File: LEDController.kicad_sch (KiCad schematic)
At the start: 16 parts, among them J1 3557-2, J10 3557-2, J11 TB001-500-04BE, J12 TB001-500-04BE, J13 TB001-500-04BE, J14 TB001-500-04BE, J15 TB001-500-04BE, J2 3557-2, J3 3557-2, J4 3557-2, J5 3557-2, J6 3557-2, J7 3557-2, J8 3557-2, J9 3557-2

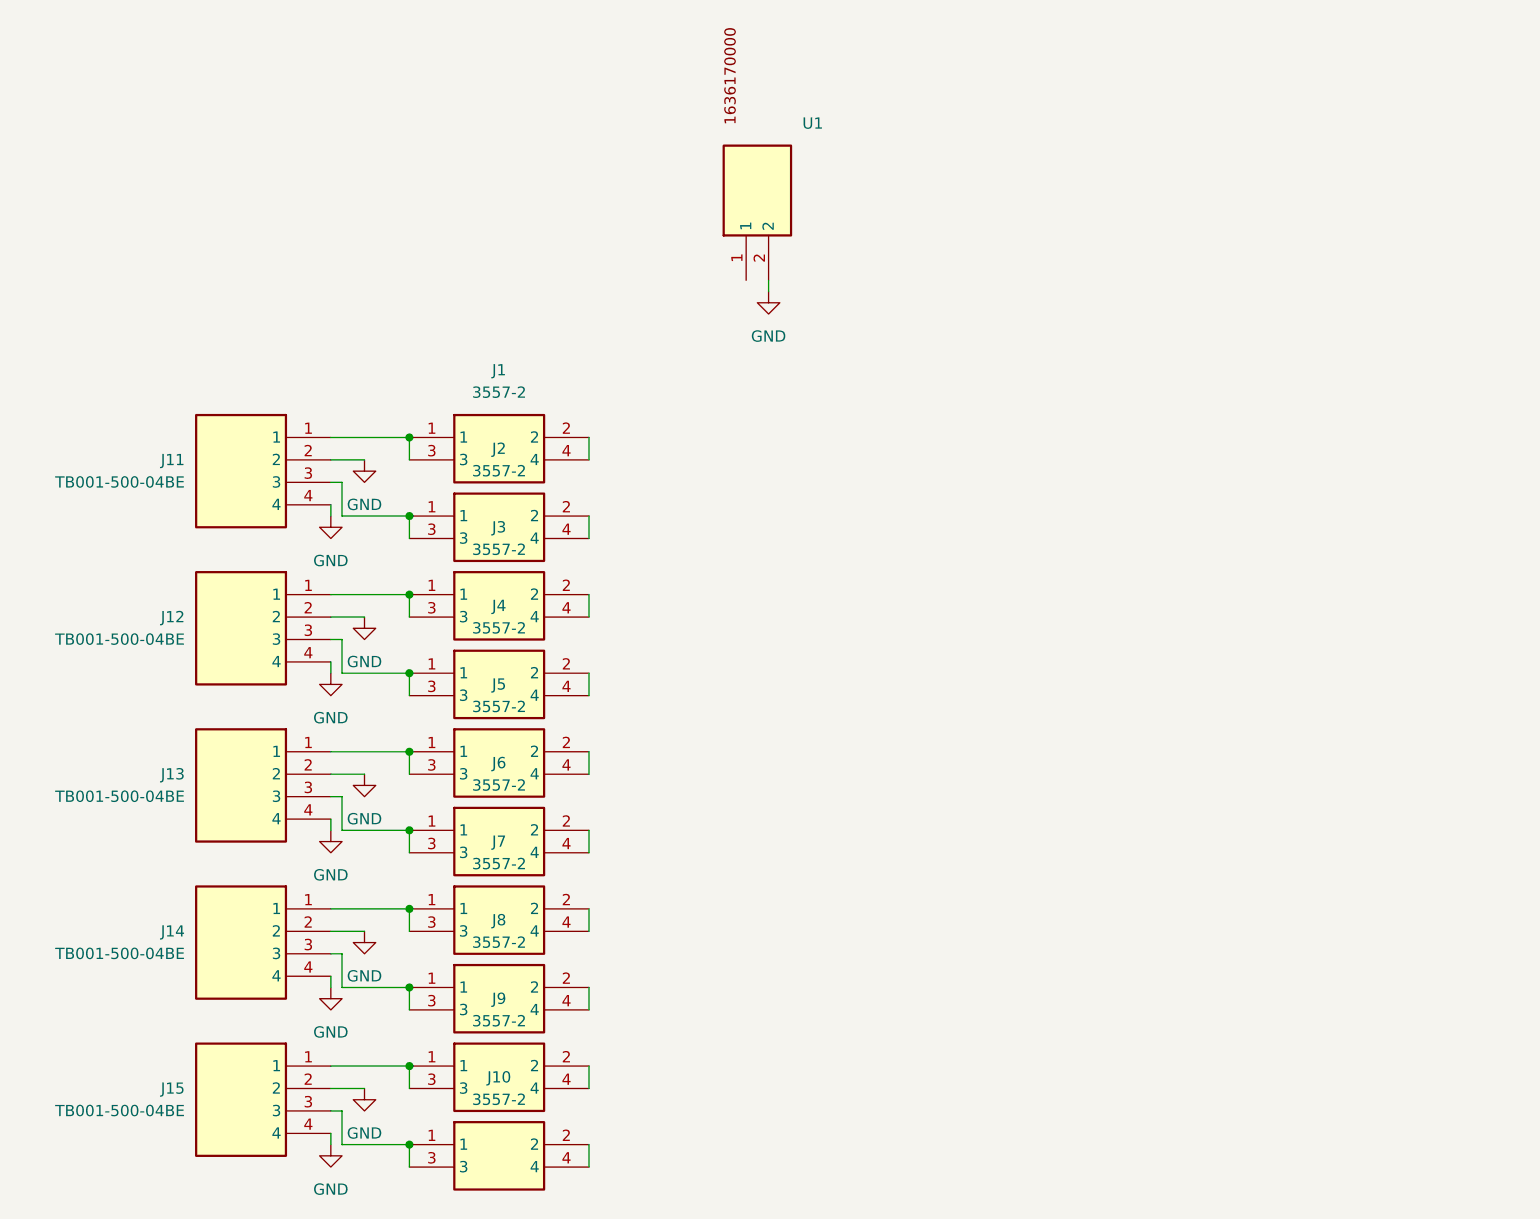
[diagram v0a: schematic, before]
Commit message: Added diode and transistor
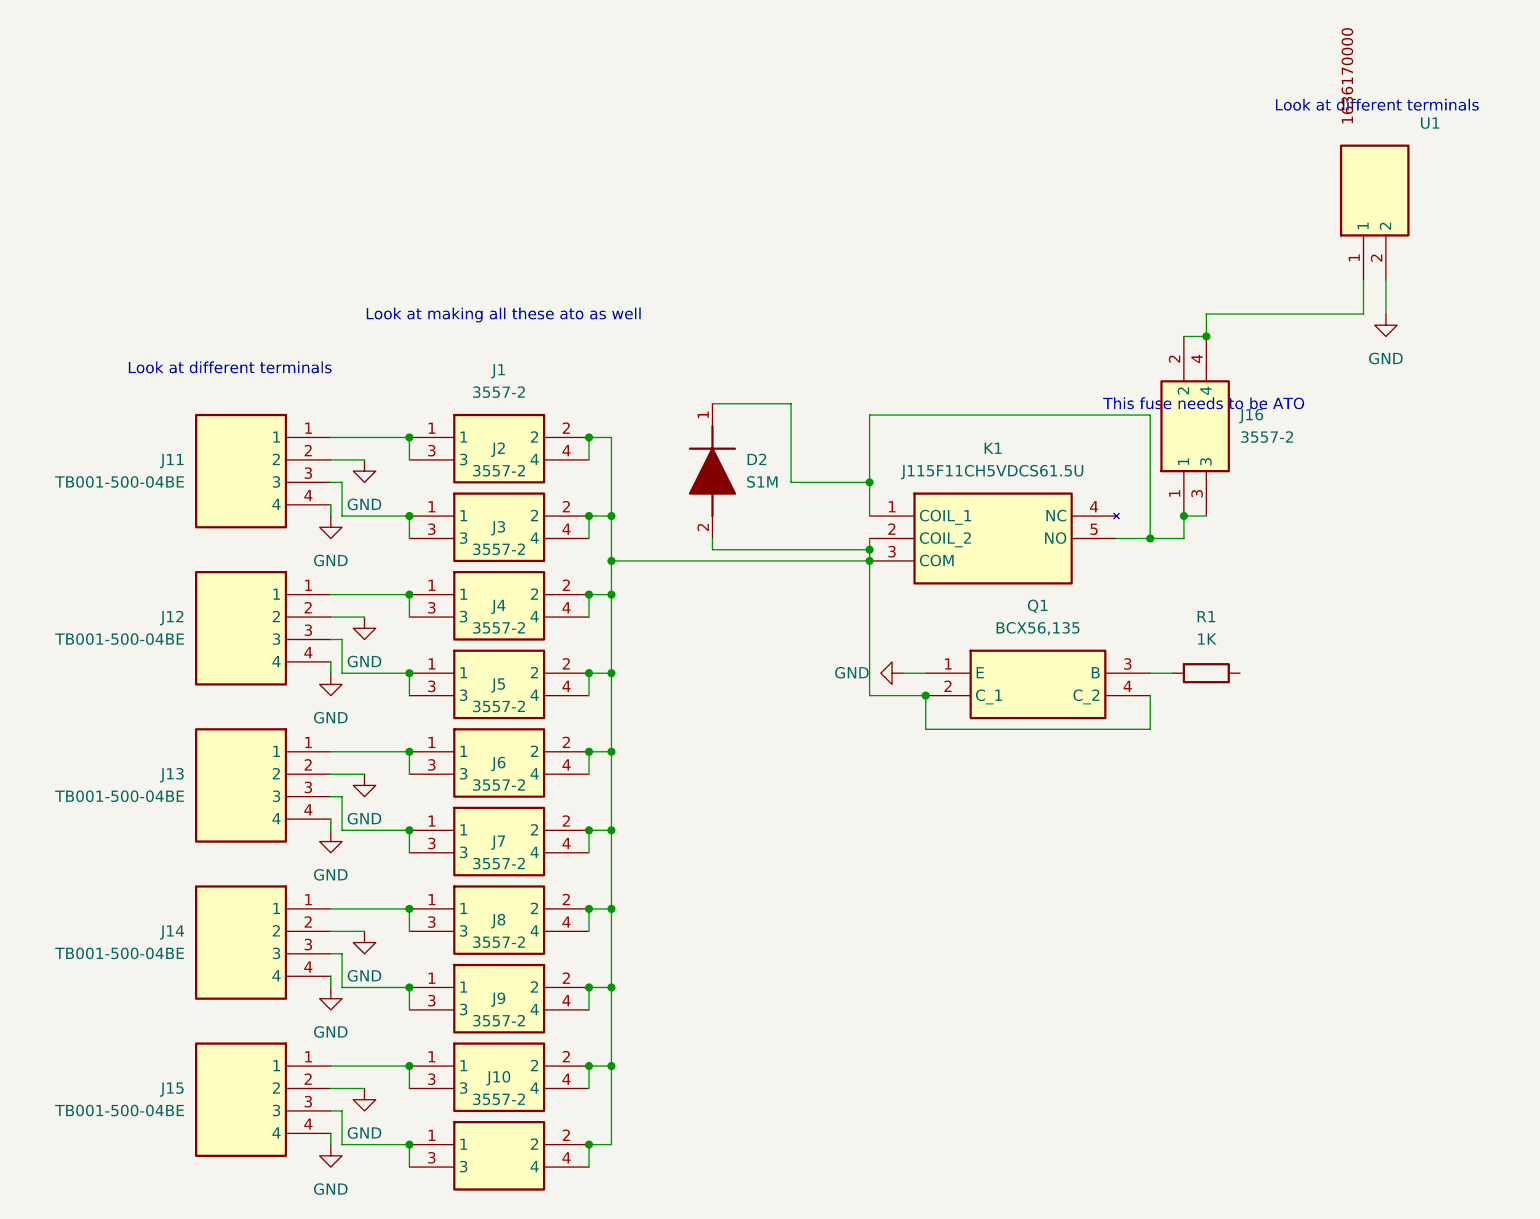
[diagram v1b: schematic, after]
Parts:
- added D2: S1M, DIOM5336X240N, symbol SamacSys_Parts:S1M
- added J16: 3557-2, 3557-2, symbol SamacSys_Parts:3557-2
- added K1: J115F11CH5VDCS61.5U, J115F11CH5VDCS615U, symbol SamacSys_Parts:J115F11CH5VDCS61.5U
- added Q1: BCX56,135, PBSS4360XX, symbol SamacSys_Parts:BCX56,135
- added R1: 1K, Resistor_SMD:R_0603_1608Metric_Pad0.98x0.95mm_HandSolder, symbol Device:R
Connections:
- net GND: now also Q1.1 (E)
- net at J2.2, J2.4: now also J1.2, J1.4, J10.2, J10.4, J3.2, J3.4, J4.2, J4.4, J5.2, J5.4, J6.2, J6.4, J7.2, J7.4, J8.2, J8.4, J9.2, J9.4, D2.2 (A), K1.2 (COIL_2), K1.3 (COM), Q1.2 (C_1), Q1.4 (C_2)
- net at U1.1: now also J16.2, J16.4
- new net: D2.1 (K), J16.1, J16.3, K1.1 (COIL_1), K1.5 (NO)
- new net: Q1.3 (B), R1.2
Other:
- note added: "Look at different terminals"
- note added: "Look at making all these ato as well"
- note added: "This fuse needs to be ATO"
- moved on the sheet: U1

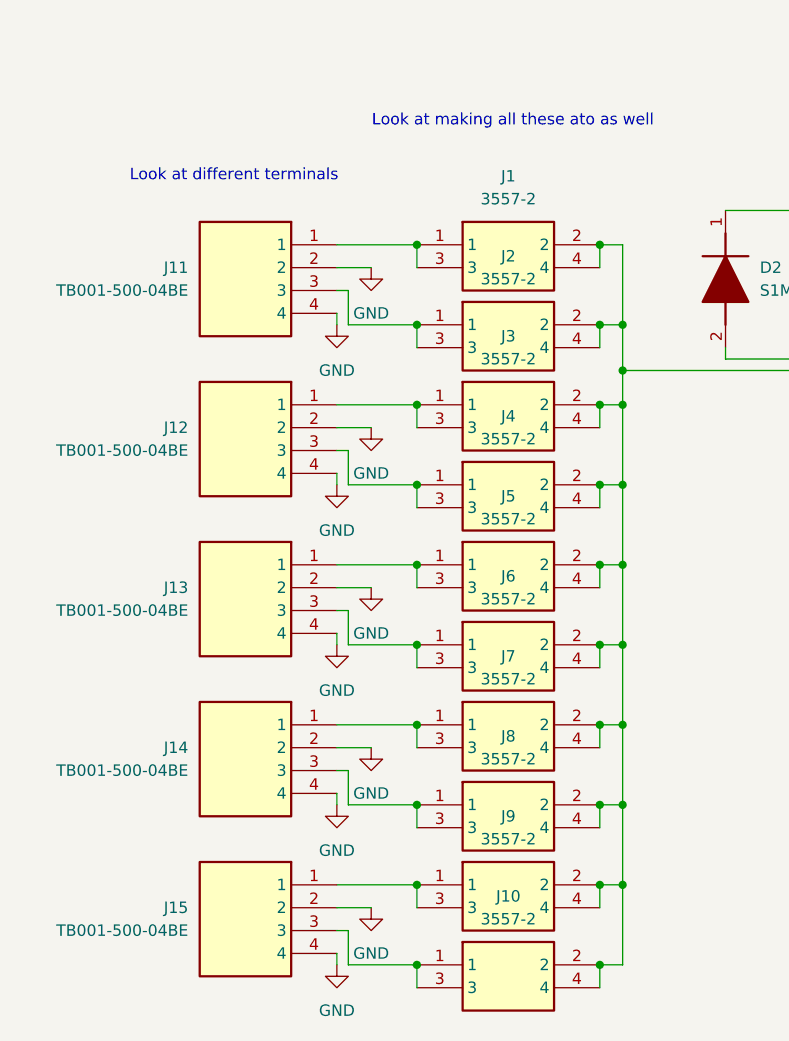
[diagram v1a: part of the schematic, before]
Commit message: Added screw terminals
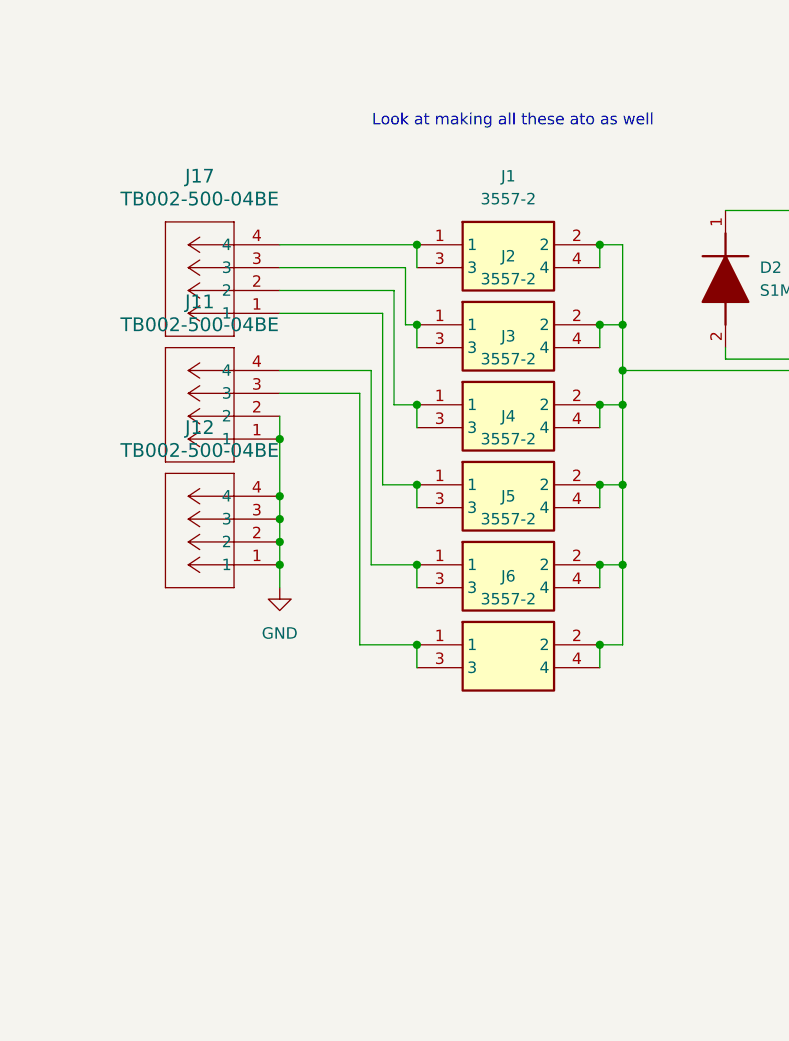
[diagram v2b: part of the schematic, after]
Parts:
- removed J10, J7, J8, J9: 3557-2, 3557-2, symbol SamacSys_Parts:3557-2
- removed J11, J12, J13, J14, J15: TB001-500-04BE, TB00150004BE, symbol SamacSys_Parts:TB001-500-04BE
- added J11, J12, J17: TB002-500-04BE, CONN4_TB002-500_787x299_CUD, symbol SamacSys_Parts:TB002-500-04BE
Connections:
- net GND: now also J11.1, J11.2, J12.1, J12.2, J12.3, J12.4
- net at J2.1, J2.3: now also J17.3
- net at J3.1, J3.3: now also J17.2
- net at J4.1, J4.3: now also J17.1
- net at J6.1, J6.3: now also J11.3
- net at J5.1, J5.3: now also J11.4
- net at J1.1, J1.3: now also J17.4

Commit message: Added new high current terminal
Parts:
- removed U1: ~, symbol SamacSys_Parts:1636170000
- added J7: VP0265840000G, CONN04_VP026584_20P32X18P3_AMP, symbol SamacSys_Parts:VP0265840000G
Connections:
- net GND: now also J7.3, J7.4
- net at J16.2, J16.4: now also J7.1, J7.2
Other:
- note removed: "Look at different terminals"
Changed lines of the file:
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@@
+	)
+	(junction
+		(at 148.59 39.37)
+		(diameter 0)
+		(color 0 0 0 0)
 	)
 	(junction
@@
 	)
 	(junction
+		(at 153.67 39.37)
+		(diameter 0)
+		(color 0 0 0 0)
+	)
+	(junction
 		(at 146.05 68.58)
 		(diameter 0)
@@
 	(wire
 		(pts
-			(xy 148.59 45.72) (xy 166.37 45.72)
-		)
-		(stroke
-			(width 0)
-			(type default)
-		)
-	)
-	(wire
-		(pts
-			(xy 166.37 45.72) (xy 166.37 41.91)
+			(xy 148.59 39.37) (xy 151.13 39.37)
 		)
 		(stroke
@@
 	(wire
 		(pts
+			(xy 153.67 39.37) (xy 156.21 39.37)
+		)
+		(stroke
+			(width 0)
+			(type default)
+		)
+	)
+	(wire
+		(pts
 			(xy 43.18 90.17) (xy 43.18 92.71)
 		)
@@
 	(wire
 		(pts
-			(xy 148.59 45.72) (xy 148.59 48.26)
+			(xy 148.59 39.37) (xy 148.59 48.26)
 		)
 		(stroke
@@
 	(wire
 		(pts
-			(xy 168.91 45.72) (xy 168.91 41.91)
-		)
-		(stroke
-			(width 0)
-			(type default)
-		)
-	)
-	(wire
-		(pts
 			(xy 78.74 77.47) (xy 81.28 77.47)
 		)
@@
 		)
 	)
-	(text "Look at different terminals\n"
-		(exclude_from_sim no)
-		(at 167.894 22.352 0)
-		(effects
-			(font
-				(size 1.27 1.27)
-			)
+	(wire
+		(pts
+			(xy 153.67 39.37) (xy 153.67 41.91)
+		)
+		(stroke
+			(width 0)
+			(type default)
 		)
 	)
@@
 	(symbol
 		(lib_id "power:GND")
-		(at 168.91 45.72 0)
+		(at 153.67 41.91 0)
 		(unit 1)
 		(exclude_from_sim no)
@@
 		(fields_autoplaced yes)
 		(property "Reference" "#PWR011"
-			(at 168.91 52.07 0)
+			(at 153.67 48.26 0)
 			(effects
 				(font
@@
 		)
 		(property "Value" "GND"
-			(at 168.91 50.8 0)
+			(at 153.67 46.99 0)
 			(effects
 				(font
@@
 		)
 		(property "Footprint" ""
-			(at 168.91 45.72 0)
+			(at 153.67 41.91 0)
 			(effects
 				(font
@@
 		)
 		(property "Datasheet" ""
-			(at 168.91 45.72 0)
+			(at 153.67 41.91 0)
 			(effects
 				(font
@@
 		)
 		(property "Description" "Power symbol creates a global label with name \"GND\" , ground"
-			(at 168.91 45.72 0)
+			(at 153.67 41.91 0)
 			(effects
 				(font
@@
 	)
 	(symbol
-		(lib_id "SamacSys_Parts:1636170000")
-		(at 166.37 41.91 90)
-		(unit 1)
-		(exclude_from_sim no)
-		(in_bom yes)
-		(on_board yes)
-		(dnp no)
-		(fields_autoplaced yes)
-		(property "Reference" "U1"
-			(at 172.72 24.162 90)
-			(effects
-				(font
-					(size 1.27 1.27)
-				)
-				(justify right)
-			)
-		)
-		(property "Value" "~"
-			(at 172.72 26.0671 90)
-			(effects
-				(font
-					(size 1.27 1.27)
-				)
-				(justify right)
-			)
-		)
-		(property "Footprint" ""
-			(at 170.18 31.75 0)
-			(effects
-				(font
-					(size 1.27 1.27)
-				)
-				(hide yes)
-			)
-		)
-		(property "Datasheet" ""
-			(at 170.18 31.75 0)
-			(effects
-				(font
-					(size 1.27 1.27)
-				)
-				(hide yes)
-			)
-		)
-		(property "Description" ""
-			(at 170.18 31.75 0)
-			(effects
-				(font
-					(size 1.27 1.27)
-				)
-				(hide yes)
-			)
-		)
-		(pin "2"
-		)
-		(pin "1"
-		)
-		(instances
-			(project ""
-				(path "/62aa0f20-cf9c-44ed-8f8b-d852f912cf95"
-					(reference "U1")
-					(unit 1)
-				)
-			)
-		)
-	)
-	(symbol
 		(lib_id "SamacSys_Parts:TB002-500-04BE")
 		(at 43.18 95.25 180)
@@
 					(unit 1)
 				)
+			)
+		)
+	)
+	(symbol
+		(lib_id "SamacSys_Parts:VP0265840000G")
+		(at 148.59 39.37 90)
+		(unit 1)
+		(exclude_from_sim no)
+		(in_bom yes)
+		(on_board yes)
+		(dnp no)
+		(fields_autoplaced yes)
+		(property "Reference" "J7"
+			(at 160.02 29.2099 90)
+			(effects
+				(font
+					(size 1.524 1.524)
+				)
+				(justify right)
+			)
+		)
+		(property "Value" "VP0265840000G"
+			(at 160.02 31.7499 90)
+			(effects
+				(font
+					(size 1.524 1.524)
+				)
+				(justify right)
+			)
+		)
+		(property "Footprint" "CONN04_VP026584_20P32X18P3_AMP"
+			(at 148.59 39.37 0)
+			(effects
+				(font
+					(size 1.27 1.27)
+					(italic yes)
+				)
+				(hide yes)
+			)
+		)
+		(property "Datasheet" "VP0265840000G"
+			(at 148.59 39.37 0)
+			(effects
+				(font
+					(size 1.27 1.27)
+					(italic yes)
+				)
+				(hide yes)
+			)
+		)
+		(property "Description" ""
+			(at 148.59 39.37 0)
+			(effects
+				(font
+					(size 1.27 1.27)
+				)
+				(hide yes)
+			)
+		)
+		(pin "1"
+		)
+		(pin "3"
+		)
+		(pin "2"
+		)
+		(pin "4"
+		)
+		(instances
+			(project ""
+				(path "/62aa0f20-cf9c-44ed-8f8b-d852f912cf95"
+					(reference "J7")
+					(unit 1)
+				)

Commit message: final schematic
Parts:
- removed J7: VP0265840000G, CONN04_VP026584_20P32X18P3_AMP, symbol SamacSys_Parts:VP0265840000G
- added C1: UVR1E102MPD, CAPPRD500W60D1025H2200, symbol SamacSys_Parts:UVR1E102MPD
- added J7: 0389690002, 0389690002, symbol SamacSys_Parts:0389690002
- added J8: 3557-2, 3557-2, symbol SamacSys_Parts:3557-2
- added J9: Conn_01x03_Pin, Connector_PinSocket_2.54mm:PinSocket_1x03_P2.54mm_Vertical, symbol Connector:Conn_01x03_Pin
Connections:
- net GND: now also C1.2 (-), J7.2, J9.3 (Pin_3)
- net at D2.2 (A), J1.2, J1.4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: now also C1.1 (+)
- net at D2.1 (K), J16.1, J16.3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: now also J8.1, J8.3, J9.2 (Pin_2)
- net at R1.1: now also J9.1 (Pin_1)
- net at J16.2, J16.4: now also J7.1, J8.2, J8.4
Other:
- note added: "These can Hold ATC, ATO, Miniature (Low Profile) (ATT)"
- note removed: "Look at making all these ato as well"
- note removed: "This fuse needs to be ATO"
- moved on the sheet: D2, J1, J11, J12, J16, J17, J2, J3, J4, J5, J6, K1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

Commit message: wip layout
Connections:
- net 50R: now reaches C1.1 (+), J1.2, J1.4, J2.2, J2.4, J3.2, J3.4, J4.2, J4.4, J5.2, J5.4, J6.2, J6.4, K1.3 (COM)
- net 50R: no longer D2.2 (A), K1.2 (COIL_2), Q1.2 (C_1), Q1.4 (C_2)
- net 50F: now reaches D2.1 (K), J16.1, J16.3, J8.1, J8.3, J9.2 (Pin_2), K1.1 (COIL_1), K1.5 (NO)
- net 50U: now reaches J16.2, J16.4, J7.1, J8.2, J8.4
- new net: D2.2 (A), K1.2 (COIL_2), Q1.2 (C_1), Q1.4 (C_2)
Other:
- moved on the sheet: C1, D2, J1, J11, J12, J16, J17, J2, J3, J4, J5, J6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
